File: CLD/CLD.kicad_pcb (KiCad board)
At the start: 2 copper layers, 35 x 32.5 mm, 30 parts, among them J1 Conn_01x02, J2 Conn_01x02, J3 Conn_01x02, J4 Conn_01x02, J5 Conn_02x05_Counter_Clockwise, Q1 BSC072N08NS5, U1 STM32F103CBUx, U2 FAN3111E, U3 INA180A1, U4 MCP2551-I-SN

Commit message: PCB
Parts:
- removed C1, C10, C2, C3, C4: 100n, Capacitor_SMD:C_0201_0603Metric
- removed C12, C5: 1u, Capacitor_SMD:C_0201_0603Metric
- added C13: 100n, Capacitor_SMD:C_0603_1608Metric, F.Cu at (130.6, 63.3)
- added L1: 0.5uH, Inductor_SMD:L_Bourns-SRN8040_8x8.15mm, F.Cu at (122.8, 67.5)
- added R7: 10, Resistor_SMD:R_0603_1608Metric, F.Cu at (131.6, 65.8)
- C11, C6, C7, C8, C9: footprint Capacitor_SMD:C_0201_0603Metric -> Capacitor_SMD:C_0603_1608Metric
- D1, D2: footprint Diode_SMD:D_0201_0603Metric -> Diode_SMD:D_0603_1608Metric
- R1: value 0.5mOhm -> 22mOhm; footprint Resistor_SMD:R_Shunt_Vishay_WSK2512_6332Metric_T1.19mm -> Resistor_SMD:R_1206_3216Metric
- R2: value 50r -> 10; footprint Resistor_SMD:R_0201_0603Metric -> Resistor_SMD:R_0603_1608Metric
- R3, R4, R5, R6: footprint Resistor_SMD:R_0201_0603Metric -> Resistor_SMD:R_0603_1608Metric
- moved C11 91.6 mm to (91.1, 64.0), turned to -135 degrees
- moved R6 82.4 mm to (83.6, 63.0), turned to -45 degrees
- moved J1 41.1 mm to (111.0, 52.8)
- moved J2 41.1 mm to (106.5, 52.8)
- moved U2 40.5 mm to (105.3, 63.6), turned to -45 degrees
- moved Q1 39.4 mm to (113.6, 66.0), turned to 180 degrees
- moved D2 33.0 mm to (98.9, 77.0), turned to 135 degrees
- moved R4 32.4 mm to (101.4, 79.5), turned to -45 degrees
- moved D1 31.4 mm to (100.4, 75.5), turned to 135 degrees
- moved C9 31.2 mm to (103.4, 72.5)
- moved R3 30.9 mm to (102.9, 78.0), turned to -45 degrees
- moved C8 30.6 mm to (93.0, 75.6)
- moved J3 30.6 mm to (92.9, 80.0)
- moved U1 30.6 mm to (96.9, 70.0)
- moved R5 27.3 mm to (83.5, 56.2), turned to 45 degrees
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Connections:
- Q1 pad 1: Net-(Q1-S-Pad1) -> Net-(L1-Pad1)
- Q1 pad 2: Net-(Q1-S-Pad1) -> Net-(L1-Pad1)
- Q1 pad 3: Net-(Q1-S-Pad1) -> Net-(L1-Pad1)
- R1 pad 1: Net-(U3-+) -> Net-(L1-Pad2)
- R2 pad 1: Net-(Q1-S-Pad1) -> Net-(L1-Pad2)
- R3 pad 1: Net-(D1-A) -> Net-(D1-K)
- R4 pad 1: Net-(D2-A) -> Net-(D2-K)
- U1 pad 13: Net-(D2-K) -> Net-(D2-A)
- U1 pad 14: Net-(D1-K) -> Net-(D1-A)
- U3 pad 4: GND -> Net-(U3--)
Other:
- board size 35 x 32.5 mm -> 56.2 x 33 mm

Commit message: howdy
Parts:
- added C1: 100n, Capacitor_SMD:C_0603_1608Metric, F.Cu at (78.7, 79.0)
- added C2: 100n, Capacitor_SMD:C_0603_1608Metric, F.Cu at (92.5, 74.0)
- added C3: 100n, Capacitor_SMD:C_0603_1608Metric, F.Cu at (92.5, 80.0)
- added D3: LED, Diode_SMD:D_0603_1608Metric, F.Cu at (85.5, 57.5)
- added R8: 50r, Resistor_SMD:R_0603_1608Metric, F.Cu at (90.0, 59.0)
- added U5: AP2112K-3.3, Package_TO_SOT_SMD:SOT-23-5, F.Cu at (92.6, 77.0)
- R3, R4: value R -> 50r
- moved C7 38.8 mm to (99.0, 74.0), turned to 180 degrees
- moved U3 36.6 mm to (99.0, 77.0), turned to 0 degrees
- moved C13 30.1 mm to (103.8, 77.0), turned to 90 degrees
- moved R7 27.9 mm to (106.5, 78.0), turned to 180 degrees
- moved J3 25.5 mm to (93.0, 54.5)
- moved R2 25.2 mm to (106.5, 76.0), turned to 180 degrees
- moved D2 21.8 mm to (113.2, 60.5), turned to 180 degrees
- moved R1 21.3 mm to (110.5, 77.0), turned to -90 degrees
- moved D1 21.3 mm to (113.2, 58.5), turned to 180 degrees
- moved J5 18.7 mm to (79.0, 60.2), turned to 180 degrees
- moved R3 17.6 mm to (98.5, 61.0), turned to 45 degrees
- moved R4 17.1 mm to (100.0, 62.5), turned to 45 degrees
- moved R5 16.1 mm to (80.4, 72.1)
- moved C9 16.1 mm to (95.5, 58.5), turned to 45 degrees
- moved R6 15.5 mm to (86.0, 78.3), turned to 45 degrees
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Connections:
- D1 pad 1: Net-(D1-K) -> GND
- D2 pad 1: Net-(D2-K) -> GND
- R3 pad 1: Net-(D1-K) -> Net-(U1-PA4)
- R3 pad 2: GND -> Net-(D1-A)
- R4 pad 1: Net-(D2-K) -> Net-(U1-PA3)
- R4 pad 2: GND -> Net-(D2-A)
- U1 pad 13: Net-(D2-A) -> Net-(U1-PA3)
- U1 pad 14: Net-(D1-A) -> Net-(U1-PA4)
- U1 pad 26: unconnected-(U1-PB13-Pad26) -> Net-(U1-PB13)
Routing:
- net GND: vias 0 -> 4
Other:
- board size 56.2 x 33 mm -> 45 x 30 mm

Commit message: PCB routed
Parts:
- moved D2 14.7 mm to (103.2, 71.2)
- moved D1 13.3 mm to (103.2, 67.2)
- moved C11 9.59 mm to (77.4, 70.5), turned to 45 degrees
- moved D3 9.46 mm to (76.2, 55.5)
- moved Q1 9.04 mm to (108.9, 60.6), turned to 0 degrees
- moved C1 6.90 mm to (85.6, 78.8), turned to 45 degrees
- moved U2 6.40 mm to (100.0, 59.0), turned to -90 degrees
- moved J2 5.97 mm to (99.1, 51.5), turned to 90 degrees
- moved R6 5.30 mm to (86.0, 73.0), turned to 135 degrees
- moved J1 4.37 mm to (109.6, 51.5)
- moved J3 3.59 mm to (91.0, 51.5)
- moved R5 3.32 mm to (83.0, 70.0), turned to 135 degrees
- moved J4 3.27 mm to (85.5, 51.5), turned to -90 degrees
- moved J5 2.85 mm to (78.3, 63.0)
- moved C9 2.71 mm to (93.0, 59.5)
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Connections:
- U1 pad 15: /Mos_EN -> unconnected-(U1-PA5-Pad15)
- U1 pad 21: unconnected-(U1-PB10-Pad21) -> /Mos_EN
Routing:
- net +3.3V: track 0.00 -> 70.4 mm, vias 0 -> 8
- net +5V: track 0.00 -> 56.4 mm, vias 0 -> 1
- net /Can_L: track 0.00 -> 25.6 mm, vias 0 -> 2
- net /Can_H: track 0.00 -> 25.2 mm, vias 0 -> 2
- net /JTAG_RST: track 0.00 -> 22.0 mm
- net GND: track 0.00 -> 20.1 mm, vias 4 -> 68
- net /JTAG_D0: track 0.00 -> 19.6 mm
- net /JTAG_SWDIO: track 0.00 -> 16.3 mm
- net /Can_Rx: track 0.00 -> 16.2 mm
- net /JTAG_D1: track 0.00 -> 15.8 mm
- net /Current: track 0.00 -> 11.9 mm
- net Net-(D3-A): track 0.00 -> 11.5 mm
- net Net-(D2-A): track 0.00 -> 10.1 mm
- net /Can_Tx: track 0.00 -> 9.61 mm
- net Net-(U3-+): track 0.00 -> 9.51 mm
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- added copper zone on B.Cu, net GND
- added copper zone on F.Cu, net GND
- added copper zone on F.Cu, net Net-(J1-Pin_2)
- added copper zone on B.Cu, net Net-(L1-Pad1)
- added copper zone on F.Cu, net Net-(L1-Pad1)
- added copper zone on F.Cu, net Net-(L1-Pad2)
- added copper zone on B.Cu, net VDD
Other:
- board size 45 x 30 mm -> 45.5 x 40 mm
- board text added: "+5V_In"
- board text added: "10A 30V"
- board text added: "5V"
- board text added: "CAN LOAD DRIVER"
- board text added: "Can"
- board text added: "Can_Bus"
- board text added: "GND"
- board text added: "HIGH"
- board text added: "IO_1"
- board text added: "IO_2"
- board text added: "LOW"
- board text added: "Load"
- board text added: "Power_In"
- board text added: "Tx/Rx"
- board text added: "VIN"

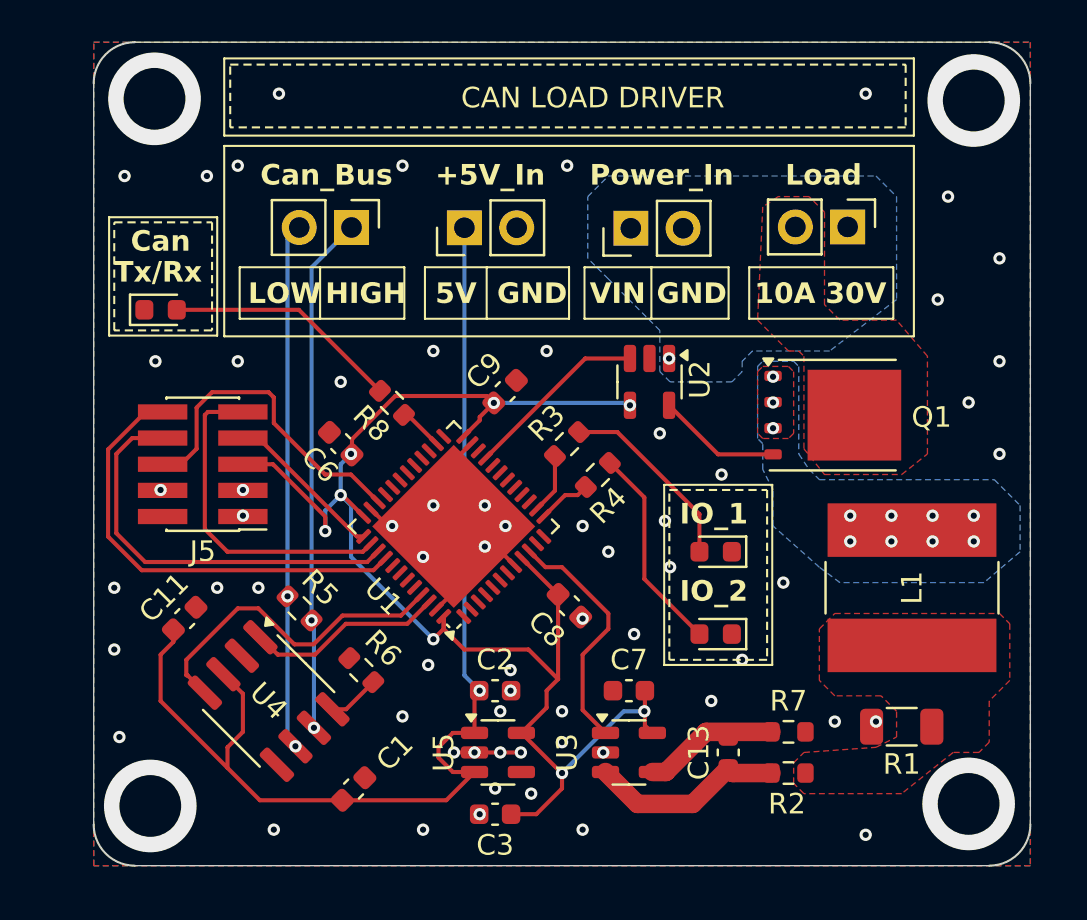
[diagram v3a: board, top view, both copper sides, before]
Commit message: add USB + crystal
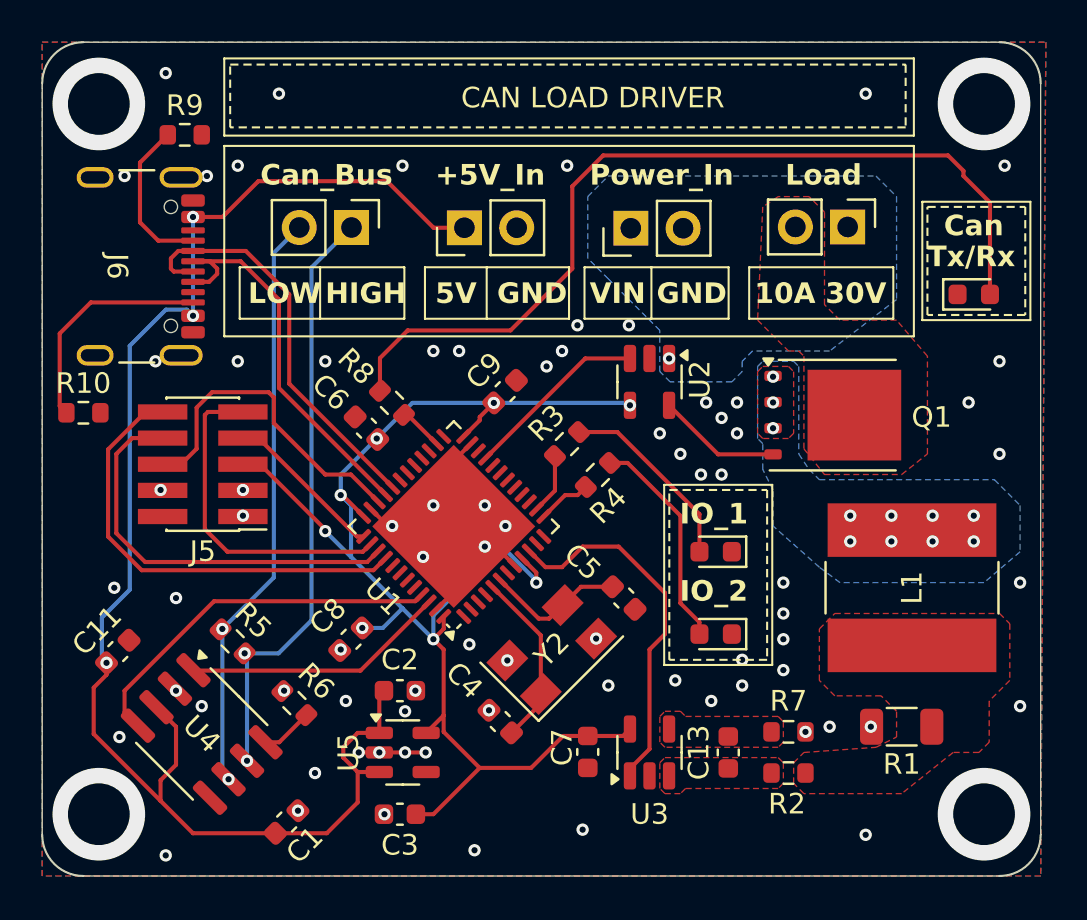
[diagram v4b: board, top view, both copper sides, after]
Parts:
- added C4: 18p, Capacitor_SMD:C_0603_1608Metric, F.Cu at (92.8, 75.5)
- added C5: 18p, Capacitor_SMD:C_0603_1608Metric, F.Cu at (98.8, 69.5)
- added J6: USB_C_Receptacle_USB2.0_14P, Connector_USB:USB_C_Receptacle_GCT_USB4105-xx-A_16P_TopMnt_Horizontal, F.Cu at (74.1, 53.4)
- added R10: 5.1k, Resistor_SMD:R_0603_1608Metric, F.Cu at (72.5, 60.5)
- added R9: 5.1k, Resistor_SMD:R_0603_1608Metric, F.Cu at (77.4, 47.0)
- added Y2: Crystal_GND24, Crystal:Crystal_SMD_Abracon_ABM3C-4Pin_5.0x3.2mm, F.Cu at (95.2, 72.0)
- moved D3 39.5 mm to (115.8, 54.8)
- moved C8 10.7 mm to (85.5, 71.5), turned to -135 degrees
- moved C2 4.62 mm to (87.9, 74.0)
- moved C3 4.62 mm to (87.9, 80.0)
- moved U5 4.62 mm to (88.0, 77.0)
- moved C1 3.62 mm to (82.4, 80.4)
- moved C11 3.62 mm to (74.2, 72.1)
- moved R5 3.62 mm to (79.8, 71.6)
- moved R6 3.62 mm to (82.8, 74.6)
- moved U4 3.62 mm to (78.2, 76.1)
- moved C7 3.58 mm to (97.0, 77.0), turned to -90 degrees
- moved C6 1.46 mm to (86.2, 61.2)
- moved U3 1.00 mm to (100.0, 77.0), turned to 90 degrees
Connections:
- U1 pad 32: unconnected-(U1-PA11-Pad32) -> /USB_DM
- U1 pad 33: unconnected-(U1-PA12-Pad33) -> /USB_DP
- U1 pad 5: unconnected-(U1-PD0-Pad5) -> Net-(U1-PD0)
- U1 pad 6: unconnected-(U1-PD1-Pad6) -> Net-(U1-PD1)
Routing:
- net Net-(D3-A): track 11.5 -> 43.2 mm
- net /USB_DM: track 0.00 -> 19.9 mm
- net /USB_DP: track 0.00 -> 19.5 mm
- net +5V: track 56.4 -> 72.3 mm, vias 1 -> 3
- net Net-(J6-CC2): track 0.00 -> 11.1 mm
- net Net-(U3-+): track 9.51 -> 0.00 mm
- net Net-(U1-PD0): track 0.00 -> 8.62 mm
- net Net-(J6-CC1): track 0.00 -> 7.75 mm
- net Net-(U1-PD1): track 0.00 -> 6.87 mm
- net Net-(U3--): track 6.60 -> 0.00 mm
- net /Current: track 11.9 -> 17.9 mm
- net /Can_H: track 25.2 -> 29.3 mm
- net /Can_L: track 25.6 -> 29.3 mm
- net /Can_Tx: track 9.61 -> 12.8 mm
- net /Can_Rx: track 16.2 -> 18.3 mm
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- added copper zone on F.Cu, net Net-(U3-+)
- added copper zone on F.Cu, net Net-(U3--)
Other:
- board size 45.5 x 40 mm -> 48.5 x 40.5 mm

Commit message: generated gerbers
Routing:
- net +3.3V: track 70.1 -> 70.2 mm, vias 8 -> 11
- net GND: vias 81 -> 89
- added copper zone on In1.Cu, net GND
- added copper zone on In2.Cu, net GND
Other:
- copper layers 2 -> 4

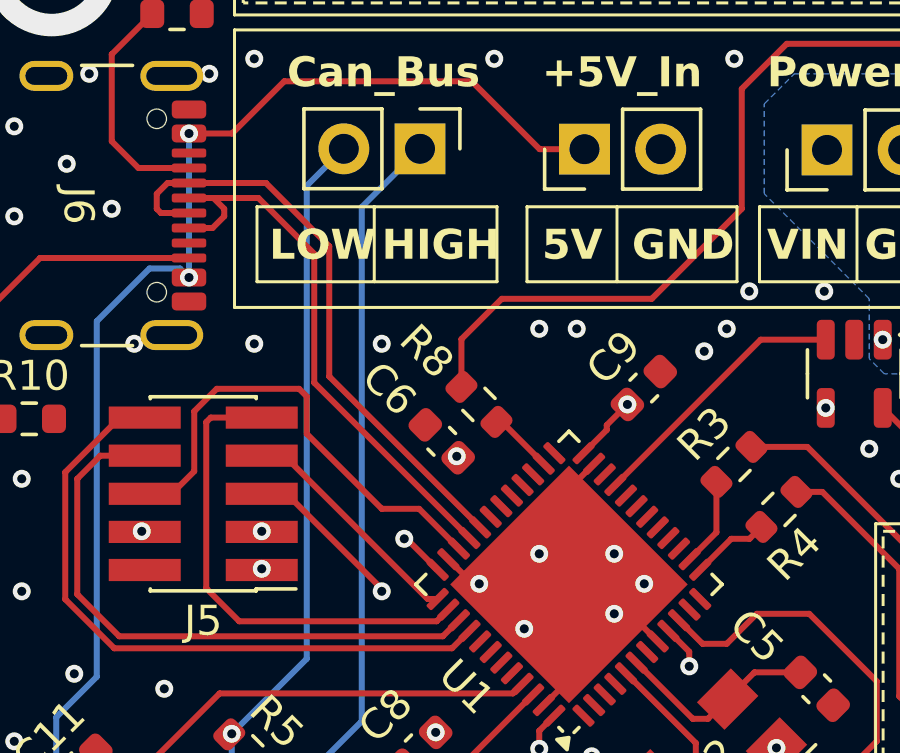
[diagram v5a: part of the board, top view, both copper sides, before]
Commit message: added USB serial resistors oops
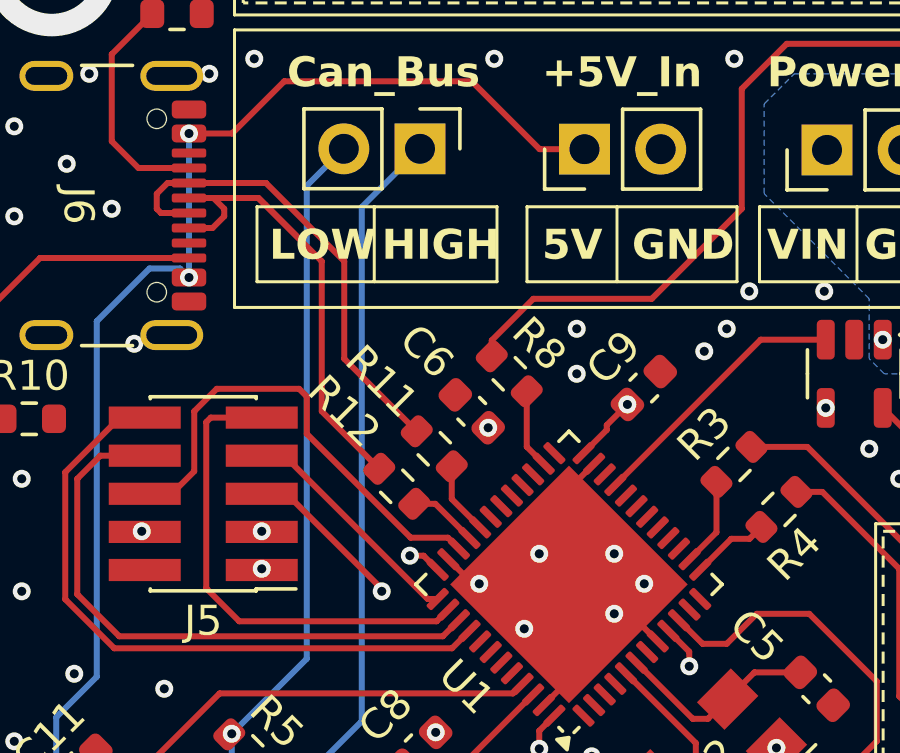
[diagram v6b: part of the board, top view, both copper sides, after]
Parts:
- added R11: 22, Resistor_SMD:R_0603_1608Metric, F.Cu at (86.0, 61.5)
- added R12: 22, Resistor_SMD:R_0603_1608Metric, F.Cu at (84.8, 62.8)
- moved R8 1.44 mm to (88.5, 59.0)
- moved C6 1.41 mm to (87.2, 60.2)
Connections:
- J6 pad A6: /USB_DP -> Net-(J6-D+-PadA6)
- J6 pad A7: /USB_DM -> Net-(J6-D--PadA7)
- J6 pad B6: /USB_DP -> Net-(J6-D+-PadA6)
- J6 pad B7: /USB_DM -> Net-(J6-D--PadA7)
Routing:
- net Net-(J6-D+-PadA6): track 0.00 -> 17.8 mm
- net /USB_DM: track 19.9 -> 2.43 mm
- net /USB_DP: track 19.5 -> 2.31 mm
- net Net-(J6-D--PadA7): track 0.00 -> 15.8 mm
- net Net-(D3-A): track 43.2 -> 41.1 mm
- net +3.3V: track 70.2 -> 69.7 mm
- net GND: vias 89 -> 87
